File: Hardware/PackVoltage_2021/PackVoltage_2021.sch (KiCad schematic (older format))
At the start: 20 parts

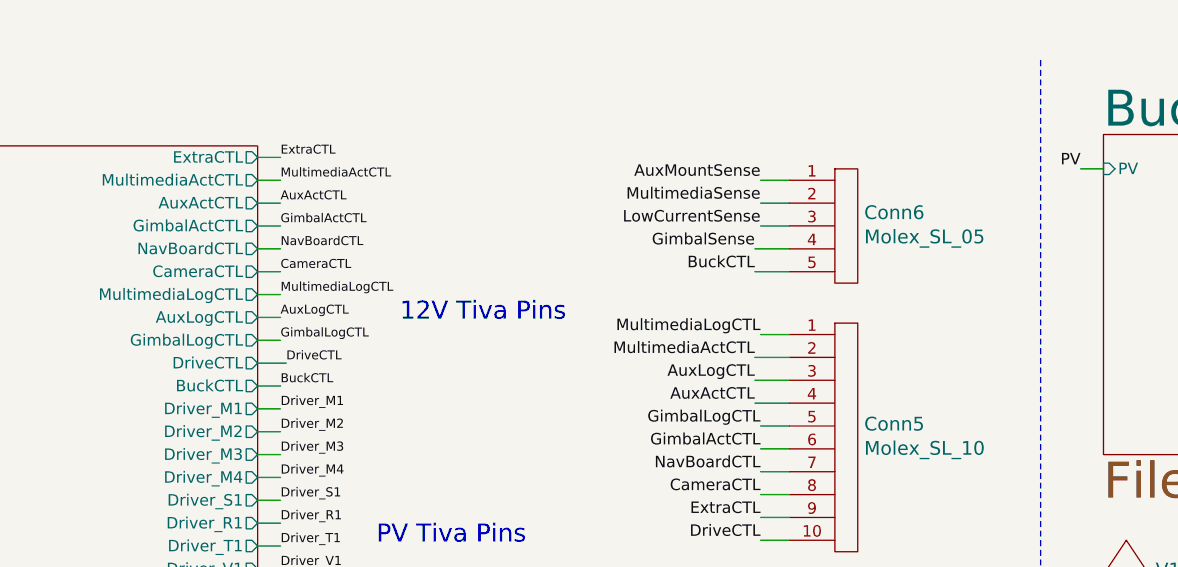
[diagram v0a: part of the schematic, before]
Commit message: molexes
- changed 5 pin molex to 4 pin molex (removed buckCTL)
- started making traces from molexes to tiva
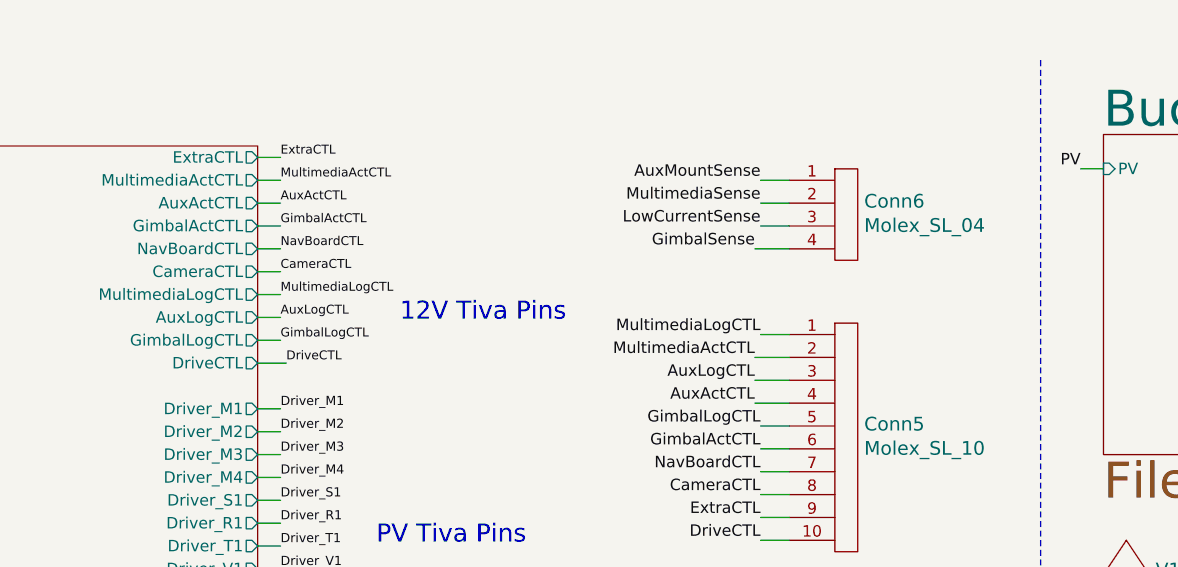
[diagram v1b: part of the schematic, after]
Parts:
- removed Conn6: Molex_SL_05, MRDT_Connectors:MOLEX_SL_05_Vertical, symbol MRDT_Connectors:Molex_SL_05
- added Conn6: Molex_SL_04, MRDT_Connectors:MOLEX_SL_04_Vertical, symbol MRDT_Connectors:Molex_SL_04
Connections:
- net AuxMountSense: now also Conn6.1
- net GimbalSense: now also Conn6.4
- net LowCurrentSense: now also Conn6.3
- net MultimediaSense: now also Conn6.2
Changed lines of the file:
@@
 F35 "DriveCTL" O R 3850 1800 50
 F36 "MultimediaLogCTL" O R 3850 1500 50
-F37 "BuckCTL" O R 3850 1900 50
 $EndSheet
 $Sheet
@@
 F4 "3V3" O R 9250 1150 50
 $EndSheet
-$Comp
-L MRDT_Connectors:Molex_SL_05 Conn6
-U 1 1 5FCEA5B7
-P 6375 1450
-F 0 "Conn6" H 6503 1758 60  0000 L CNN
-F 1 "Molex_SL_05" H 6503 1652 60  0000 L CNN
-F 2 "MRDT_Connectors:MOLEX_SL_05_Vertical" H 6375 1450 60  0001 C CNN
-F 3 "" H 6375 1450 60  0001 C CNN
-	1    6375 1450
-	1    0    0    -1
-$EndComp
-Wire Wire Line
-	6175 1400 6025 1400
-Text Label 6025 1400 2    50   ~ 0
-BuckCTL
-Text Label 3950 1900 0    39   ~ 0
-BuckCTL
-Wire Wire Line
-	3950 1900 3850 1900
 Connection ~ 9800 3325
 Wire Wire Line
@@
 Text Label 6050 2375 2    50   ~ 0
 CameraCTL
+$Comp
+L MRDT_Connectors:Molex_SL_04 Conn6
+U 1 1 607586C8
+P 6375 1350
+F 0 "Conn6" H 6503 1608 60  0000 L CNN
+F 1 "Molex_SL_04" H 6503 1502 60  0000 L CNN
+F 2 "MRDT_Connectors:MOLEX_SL_04_Vertical" H 6375 1350 60  0001 C CNN
+F 3 "" H 6375 1350 60  0001 C CNN
+	1    6375 1350
+	1    0    0    -1
+$EndComp
 $EndSCHEMATC
